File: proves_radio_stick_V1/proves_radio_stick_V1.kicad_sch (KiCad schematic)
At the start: 49 parts, among them IC2 AZ1117CH-3.3TRG1, J12 USB_C_Receptacle_USB2.0_16P, J22 SWD Port, SW1 KMR2, SW2 KMR2, SW3 SW_Push_SPDT, U11 W25Q128JVS, U18 RP2350_60QFN, Y1 ABM8-272-T3

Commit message: Added E22-400M
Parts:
- added U1: E22-400M30S, easyeda2kicad:WIRELM-SMD_E22-400M30S, symbol easyeda2kicad:E22-400M30S
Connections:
- net GND: now also U1.1 (GND), U1.11 (GND), U1.12 (GND), U1.2 (GND), U1.20 (GND), U1.22 (GND), U1.3 (GND), U1.4 (GND), U1.5 (GND)
- new net: U1.10 (VCC), U1.9 (VCC)
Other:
- moved on the sheet: C12, C13, D3, D4, IC2, J12, R10, R25, R26, R27, R39, R41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

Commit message: Initial TPS62 Layout
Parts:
- added C14: 22uF, Capacitor_SMD:C_0603_1608Metric, symbol Adafruit ItsyBitsy RP2040-eagle-import:CAP_CERAMIC_0603MP
- added C15: 10uF, Capacitor_SMD:C_0603_1608Metric, symbol Adafruit ItsyBitsy RP2040-eagle-import:CAP_CERAMIC_0603MP
- added L1: XFL4015-471MEC, easyeda2kicad:IND-SMD_L4.0-W4.0_XFL4020-102MEB, symbol easyeda2kicad:XFL4015-471MEC
- added R3: 162k, Resistor_SMD:R_0603_1608Metric, symbol mainboard:RESISTOR0603
- added R4: 510k, Resistor_SMD:R_0603_1608Metric, symbol mainboard:RESISTOR0603
- added U2: TPS62085RLTT, easyeda2kicad:VSON-7_L2.0-W2.0-P0.5-TL, symbol easyeda2kicad:TPS62085RLTT
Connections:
- net +3V3: now also C14.1, L1.2, R4.1, U2.4 (VOS)
- net GND: now also C14.2, C15.2, R3.2, U2.5 (GND)
- net VBUS: now also C15.1, U2.1 (EN), U2.7 (VIN)
- new net: R3.1, R4.2, U2.3 (FB)
- new net: L1.1, U2.6 (SW)
- no-connect marks 3 -> 4

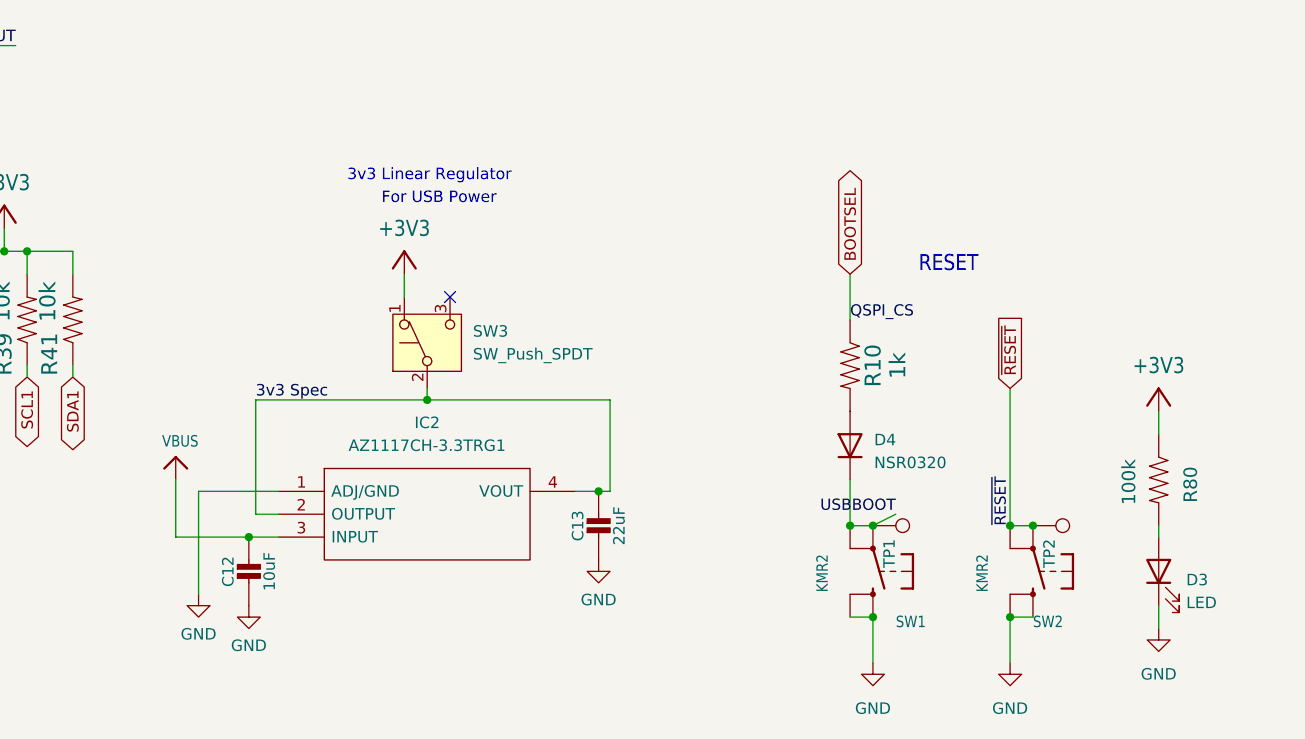
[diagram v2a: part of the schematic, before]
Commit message: Removed 3v3 Linear Regulator
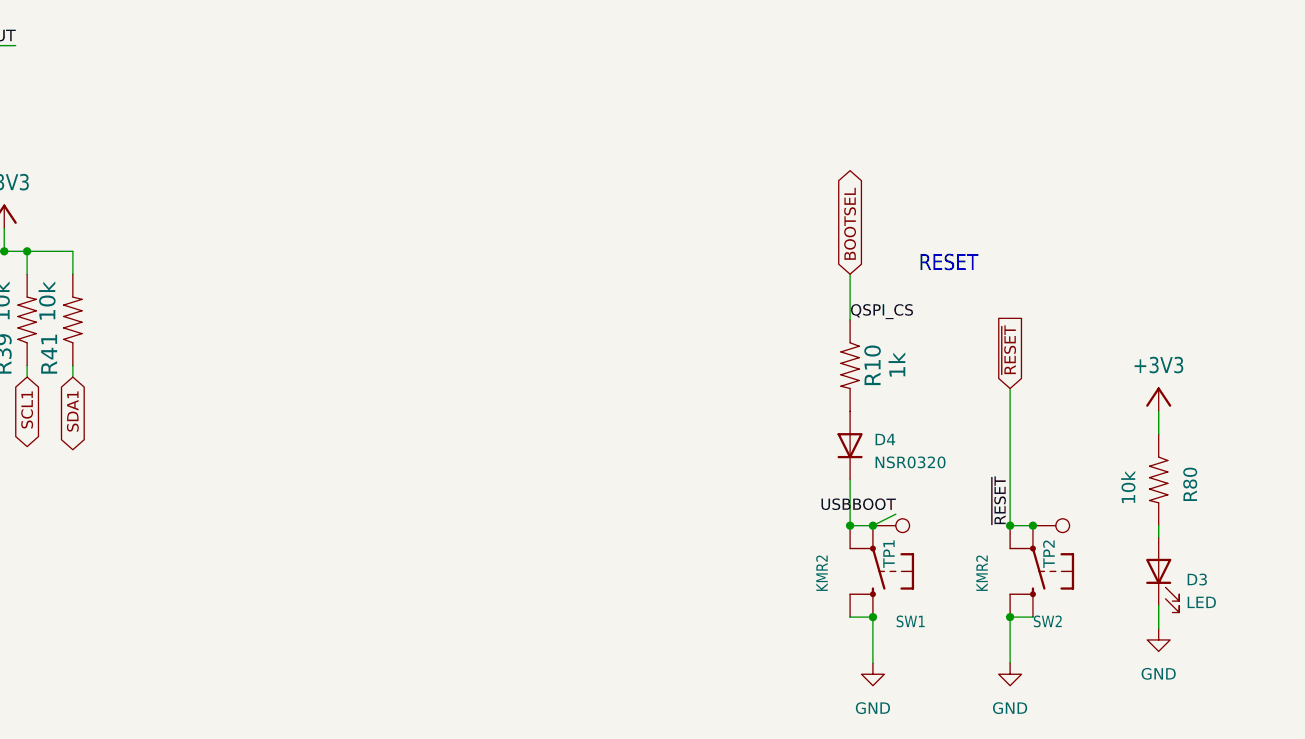
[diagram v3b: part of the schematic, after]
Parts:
- removed C12: 10uF, Capacitor_SMD:C_0603_1608Metric, symbol Adafruit ItsyBitsy RP2040-eagle-import:CAP_CERAMIC_0603MP
- removed C13: 22uF, Capacitor_SMD:C_0603_1608Metric, symbol Adafruit ItsyBitsy RP2040-eagle-import:CAP_CERAMIC_0603MP
- removed IC2: AZ1117CH-3.3TRG1, Package_TO_SOT_SMD:SOT-223, symbol AZ1117CH-3.3TRG1:AZ1117CH-3.3TRG1
- removed SW3: SW_Push_SPDT, easyeda2kicad:SW-TH_SHOU-HAN_SS12D10G4, symbol Switch:SW_Push_SPDT
- R80: value 100k -> 10k
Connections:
- no-connect marks 4 -> 3
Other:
- note removed: "3v3 Linear Regulator"
- note removed: "For USB Power"

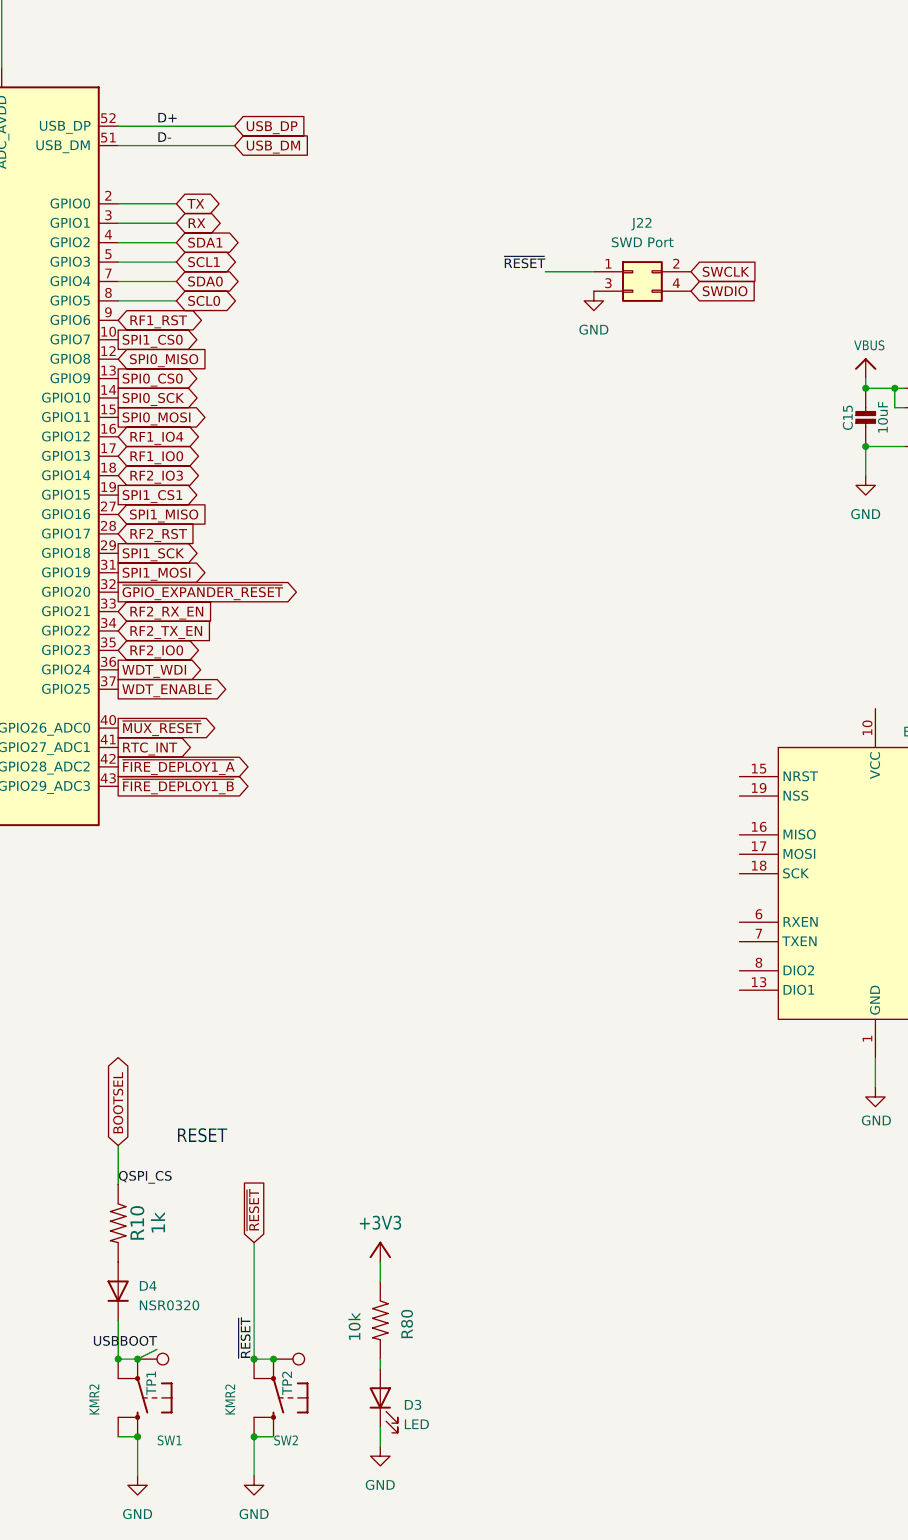
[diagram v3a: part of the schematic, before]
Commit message: RP2350 and Support Circuits Layout
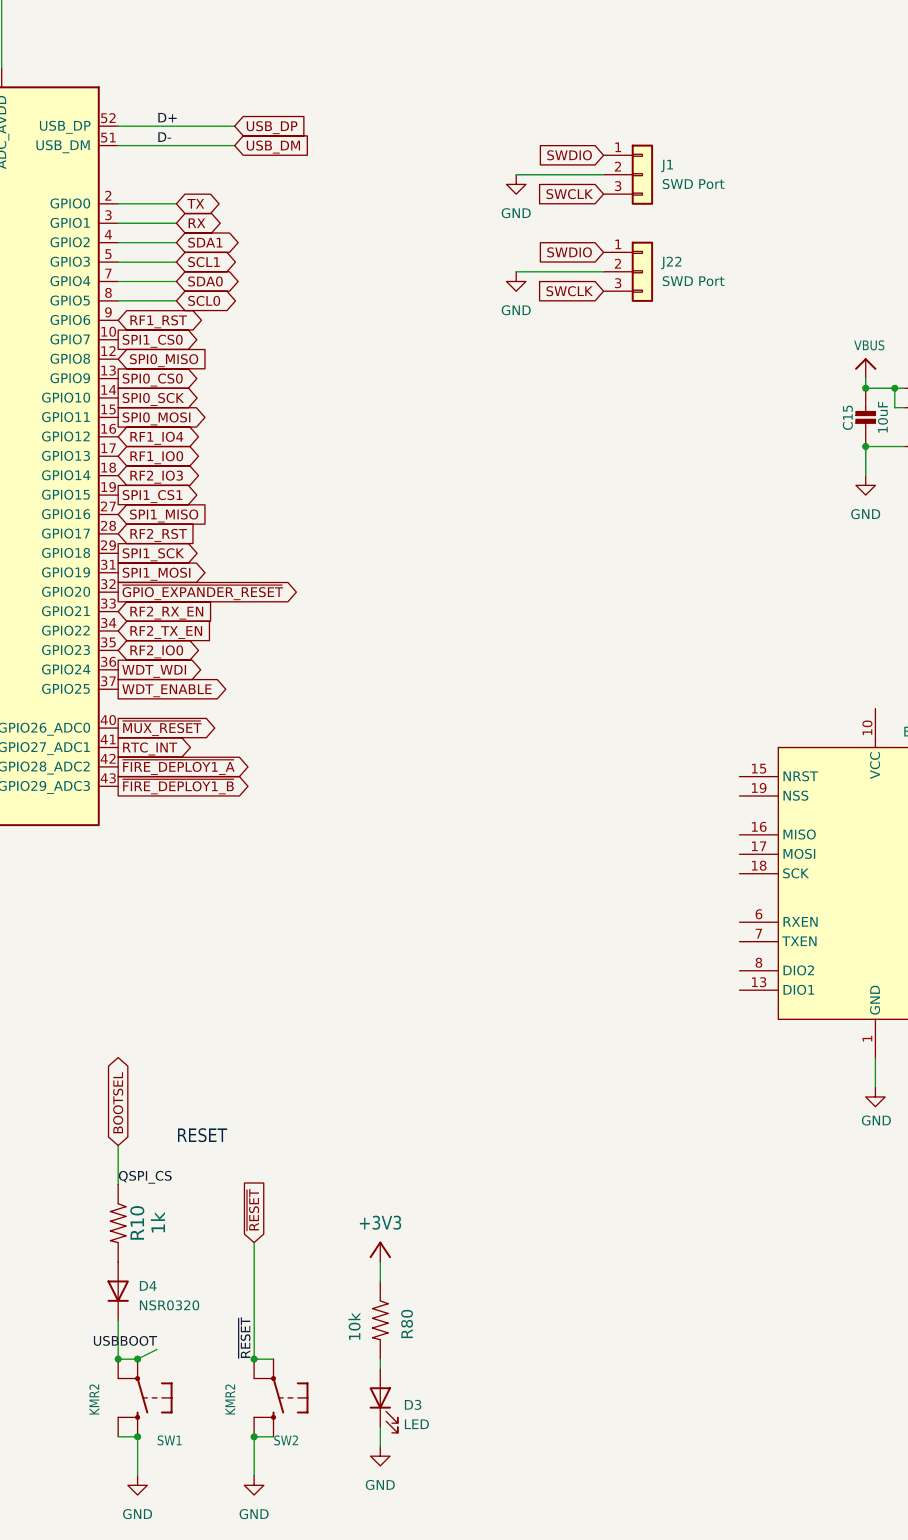
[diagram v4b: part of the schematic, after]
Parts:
- removed TP1: USBBOOT, TestPoint:TestPoint_Loop_D1.80mm_Drill1.0mm_Beaded, symbol Connector:TestPoint
- removed TP2: RESET, TestPoint:TestPoint_Loop_D1.80mm_Drill1.0mm_Beaded, symbol Connector:TestPoint
- added J1: SWD Port, Connector_PinHeader_2.54mm:PinHeader_1x03_P2.54mm_Vertical, symbol Connector_Generic:Conn_01x03
- C75: footprint Capacitor_SMD:C_0805_2012Metric -> Capacitor_SMD:C_0603_1608Metric
- J22: footprint Connector_PinHeader_1.27mm:PinHeader_2x02_P1.27mm_Vertical -> Connector_JST:JST_SH_BM03B-SRSS-TB_1x03-1MP_P1.00mm_Vertical; symbol Connector_Generic:Conn_02x02_Odd_Even -> Connector_Generic:Conn_01x03
- R1, R10, R25, R26, R27, R3, R39, R4, R41, R6, R7, R8, R80: footprint Resistor_SMD:R_0603_1608Metric -> Resistor_SMD:R_0402_1005Metric
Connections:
- net FC_RESET: no longer J22.1 (Pin_1)
- net GND: now also J22.2 (Pin_2), J1.2 (Pin_2); no longer J22.3 (Pin_3)
- net SWCLK: now also J22.3 (Pin_3), J1.3 (Pin_3); no longer J22.2 (Pin_2)
- net SWDIO: now also J22.1 (Pin_1), J1.1 (Pin_1); no longer J22.4 (Pin_4)

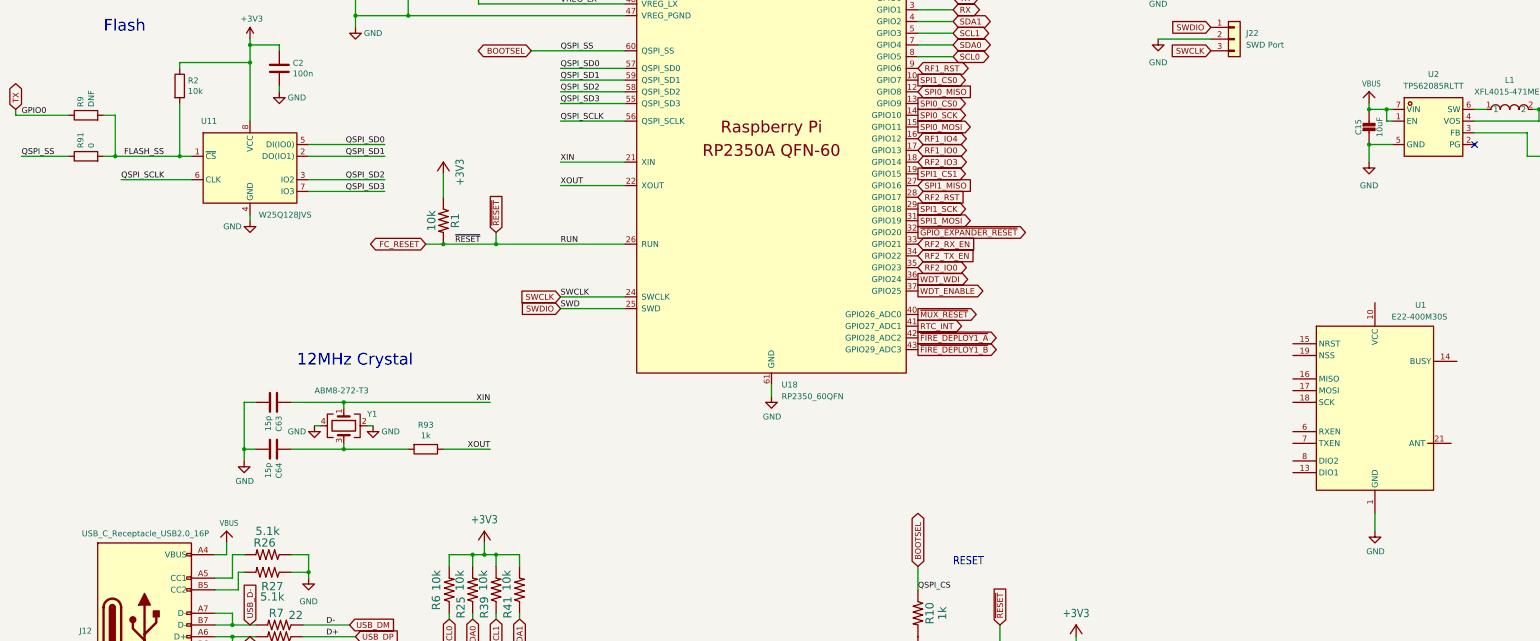
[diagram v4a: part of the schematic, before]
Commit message: Added E32 Footprint
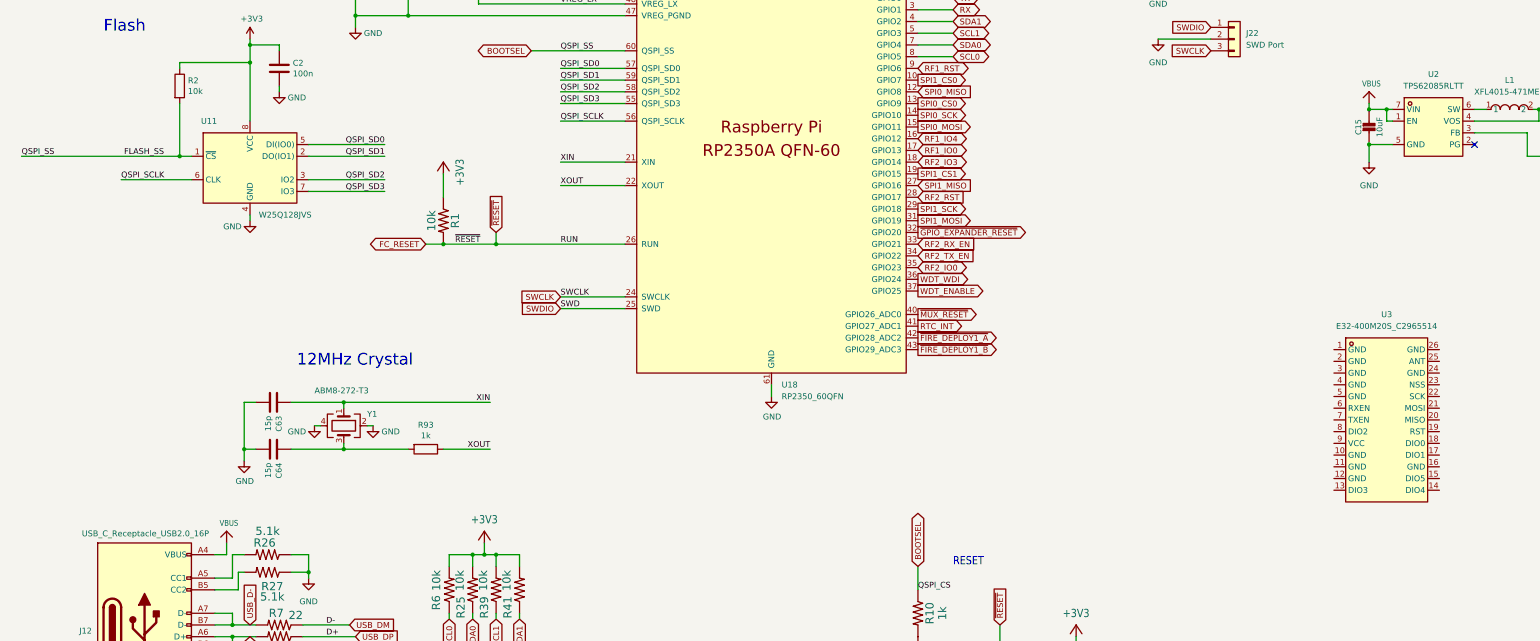
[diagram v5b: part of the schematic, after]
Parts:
- removed R9: DNF, Resistor_SMD:R_0402_1005Metric, symbol Device:R
- removed R91: 0, Resistor_SMD:R_0402_1005Metric, symbol Device:R
- removed U1: E22-400M30S, easyeda2kicad:WIRELM-SMD_E22-400M30S, symbol easyeda2kicad:E22-400M30S
- added U3: E32-400M20S_C2965514, easyeda2kicad:WIRELM-SMD_E32-400M20S, symbol easyeda2kicad:E32-400M20S_C2965514
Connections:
- net FLASH_SS is gone; now on net BOOTSEL: R2.2, U11.1 (~{CS})

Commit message: Initial Layout Complete
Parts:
- added C1: 100n, Capacitor_SMD:C_0402_1005Metric, symbol Device:C
- added C3: 47uF, Capacitor_SMD:C_0603_1608Metric, symbol Device:C
- added H1, H2, H3, H4: MountingHole, MountingHole:MountingHole_2.2mm_M2_Pad_Via, symbol Mechanical:MountingHole
- added J2: Conn_Coaxial, Connector_Coaxial:SMA_Amphenol_132134_Vertical, symbol Connector:Conn_Coaxial
- added R11, R12, R5, R9: 10k, Resistor_SMD:R_0402_1005Metric, symbol mainboard:RESISTOR0603
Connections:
- net RF2_IO3 is gone; now on net RF1_IO0: U18.18 (GPIO14)
- net RF2_RST is gone; now on net RF1_IO3: U18.28 (GPIO17)
- net RF2_RX_EN is gone; now on net RF1_TX_EN: U18.33 (GPIO21)
- net SPI0_CS0 is gone; now on net SPI1_CS0: U18.13 (GPIO9)
- net SPI0_MISO is gone; now on net SPI1_MISO: U18.12 (GPIO8)
- net SPI0_MOSI is gone; now on net SPI1_MOSI: U18.15 (GPIO11)
- net SPI0_SCK is gone; now on net SPI1_SCK: U18.14 (GPIO10)
- net SPI1_CS1 is gone; now on net RF1_IO1: U18.19 (GPIO15)
- net ~{GPIO_EXPANDER_RESET} is gone; now on net RF1_RX_EN: U18.32 (GPIO20)
- net +3V3: now also U3.9 (VCC), C1.1, C3.1, R5.2, R9.2
- net GND: now also U3.1 (GND), U3.10 (GND), U3.11 (GND), U3.12 (GND), U3.16 (GND), U3.2 (GND), U3.24 (GND), U3.26 (GND), U3.3 (GND), U3.4 (GND), U3.5 (GND), C1.2, C3.2, J2.2 (Ext), R11.1, R12.1
- net RF1_IO0: now also U3.18 (DIO0); no longer U18.17 (GPIO13)
- net RF1_IO4: now also U18.29 (GPIO18), U3.14 (DIO4); no longer U18.16 (GPIO12)
- net RF1_RST: now also U3.19 (RST), R5.1
- net SPI1_CS0: now also U3.23 (NSS), R9.1; no longer U18.10 (GPIO7)
- net SPI1_MISO: now also U3.20 (MISO); no longer U18.27 (GPIO16)
- net SPI1_MOSI: now also U3.21 (MOSI); no longer U18.31 (GPIO19)
- net SPI1_SCK: now also U3.22 (SCK); no longer U18.29 (GPIO18)
- net RF1_IO3: now reaches U3.13 (DIO3)
- net RF1_IO5: now reaches U3.15 (DIO5)
- net RF1_IO5: now also U18.31 (GPIO19)
- net RF1_IO1: now reaches U3.17 (DIO1)
- net at U3.25 (ANT): now also J2.1 (In)
- net RF1_RX_EN: now reaches U3.6 (RXEN)
- net RF1_RX_EN: now also R11.2
- net RF1_TX_EN: now reaches U3.7 (TXEN)
- net RF1_TX_EN: now also R12.2
- net RF1_IO2: now reaches U3.8 (DIO2)
- net RF1_IO2: now also U18.27 (GPIO16)
- net RF2_IO0: no longer names the net of U18.35 (GPIO23)
- net RF2_TX_EN: no longer names the net of U18.34 (GPIO22)
- net RTC_INT: no longer names the net of U18.41 (GPIO27_ADC1)
- net WDT_ENABLE: no longer names the net of U18.37 (GPIO25)
- net WDT_WDI: no longer names the net of U18.36 (GPIO24)
- net ~{FIRE_DEPLOY1_A}: no longer names the net of U18.42 (GPIO28_ADC2)
- net ~{FIRE_DEPLOY1_B}: no longer names the net of U18.43 (GPIO29_ADC3)
- net ~{MUX_RESET}: no longer names the net of U18.40 (GPIO26_ADC0)
